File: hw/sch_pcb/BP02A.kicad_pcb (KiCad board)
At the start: 2 copper layers, 60.5 x 40.1 mm, 38 parts, among them J1 SATA7-67491-1030, J2 SATA7-67491-1030, M1 HOLE, M2 HOLE, M3 HOLE, M4 HOLE

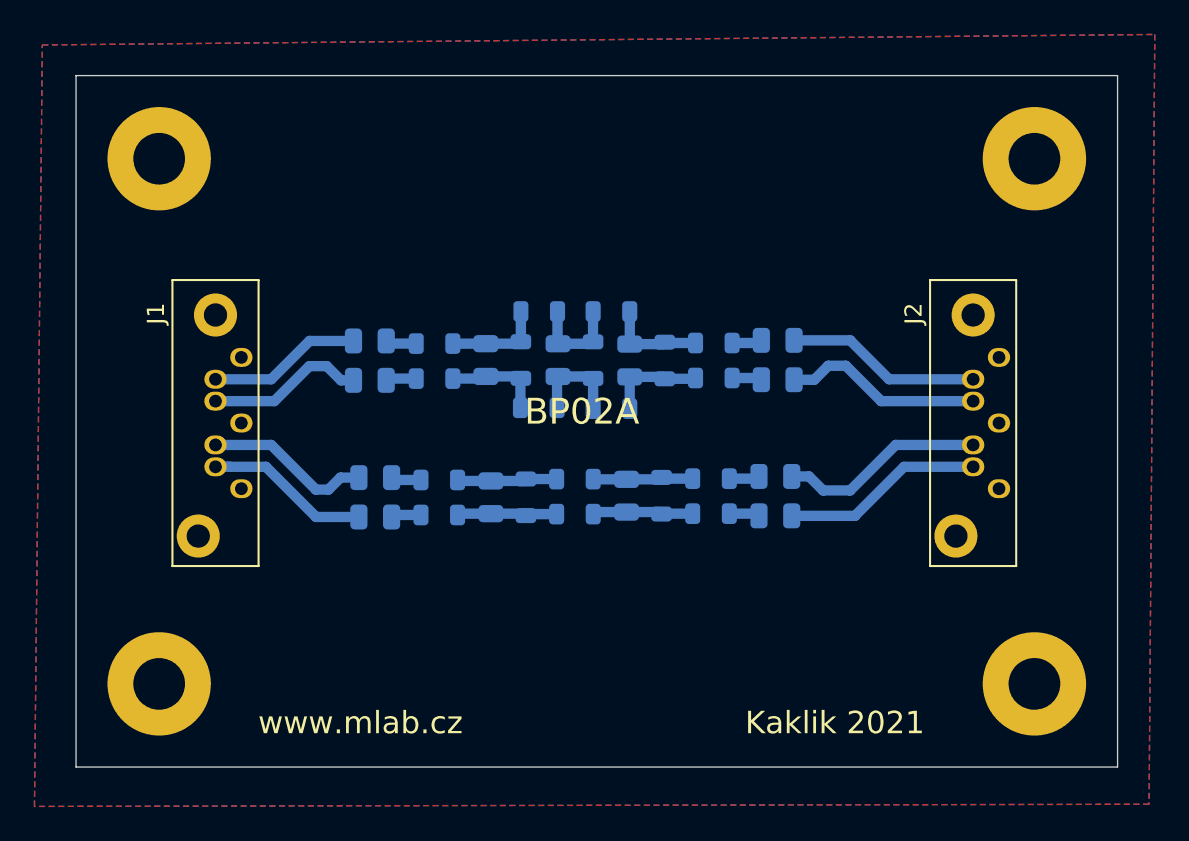
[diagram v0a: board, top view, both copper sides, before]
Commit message: Improve silksceen Resolve #1.
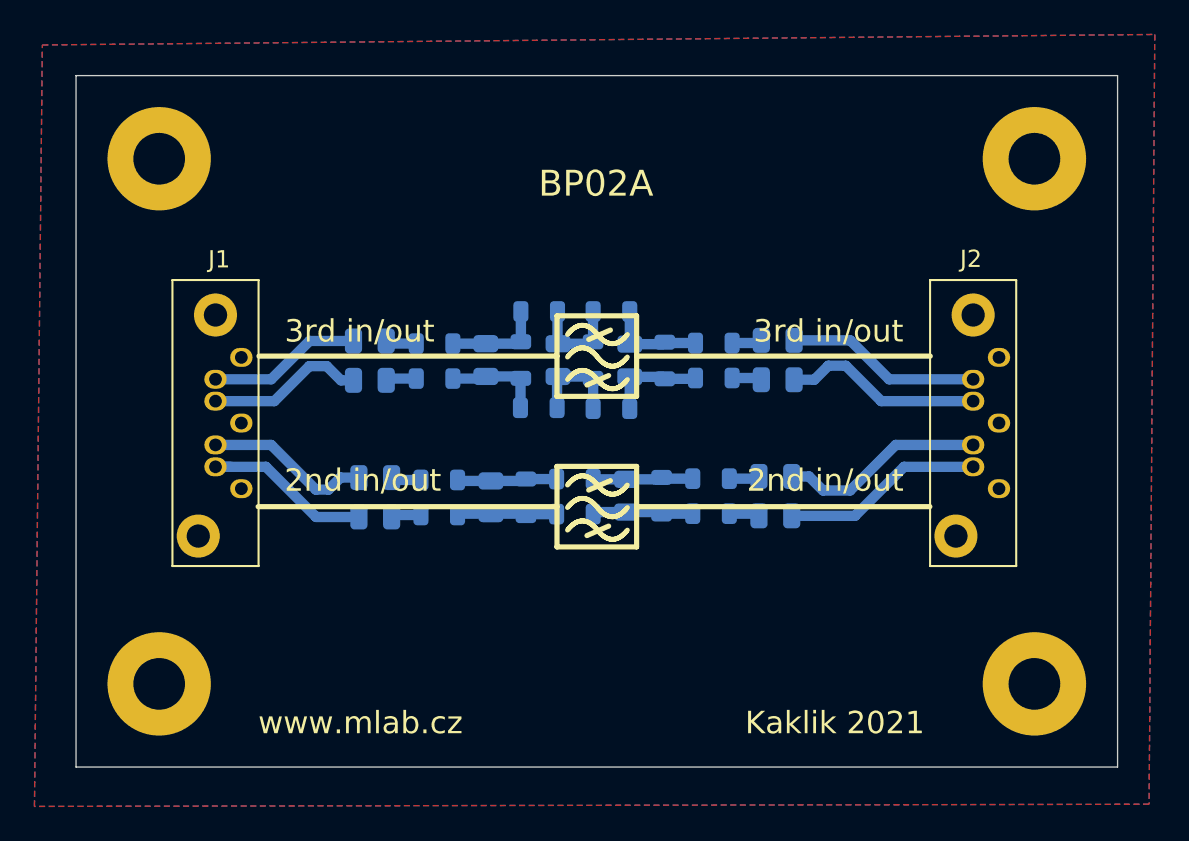
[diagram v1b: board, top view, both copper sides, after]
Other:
- board text added: "2nd in/out"
- board text added: "3rd in/out"

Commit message: Výrobní data
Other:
- rule pad_to_mask_clearance: 0 -> 0.2
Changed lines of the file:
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@@
-(kicad_pcb (version 20210424) (generator pcbnew)
+(kicad_pcb (version 20210228) (generator pcbnew)
   (general
     (thickness 1.6)
@@
       (dielectric_constraints no)
     )
-    (pad_to_mask_clearance 0)
+    (pad_to_mask_clearance 0.2)
     (pcbplotparams
       (layerselection 0x00010e0_ffffffff)
